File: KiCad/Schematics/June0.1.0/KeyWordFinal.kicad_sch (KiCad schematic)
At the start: 56 parts, among them J1 USB4105-GF-A, J2 Conn_01x02_Pin, J3 Conn_01x05_Pin, J4 MSD-10-C, U1 NRF52805-CAAA-R, U2 NPM1100-CAAA-R7, U3 TXB0104RUTR, U4 TPS62743YFPR, U5 MCP6142T-E/MS, Y1 32.868k, Y3 32M

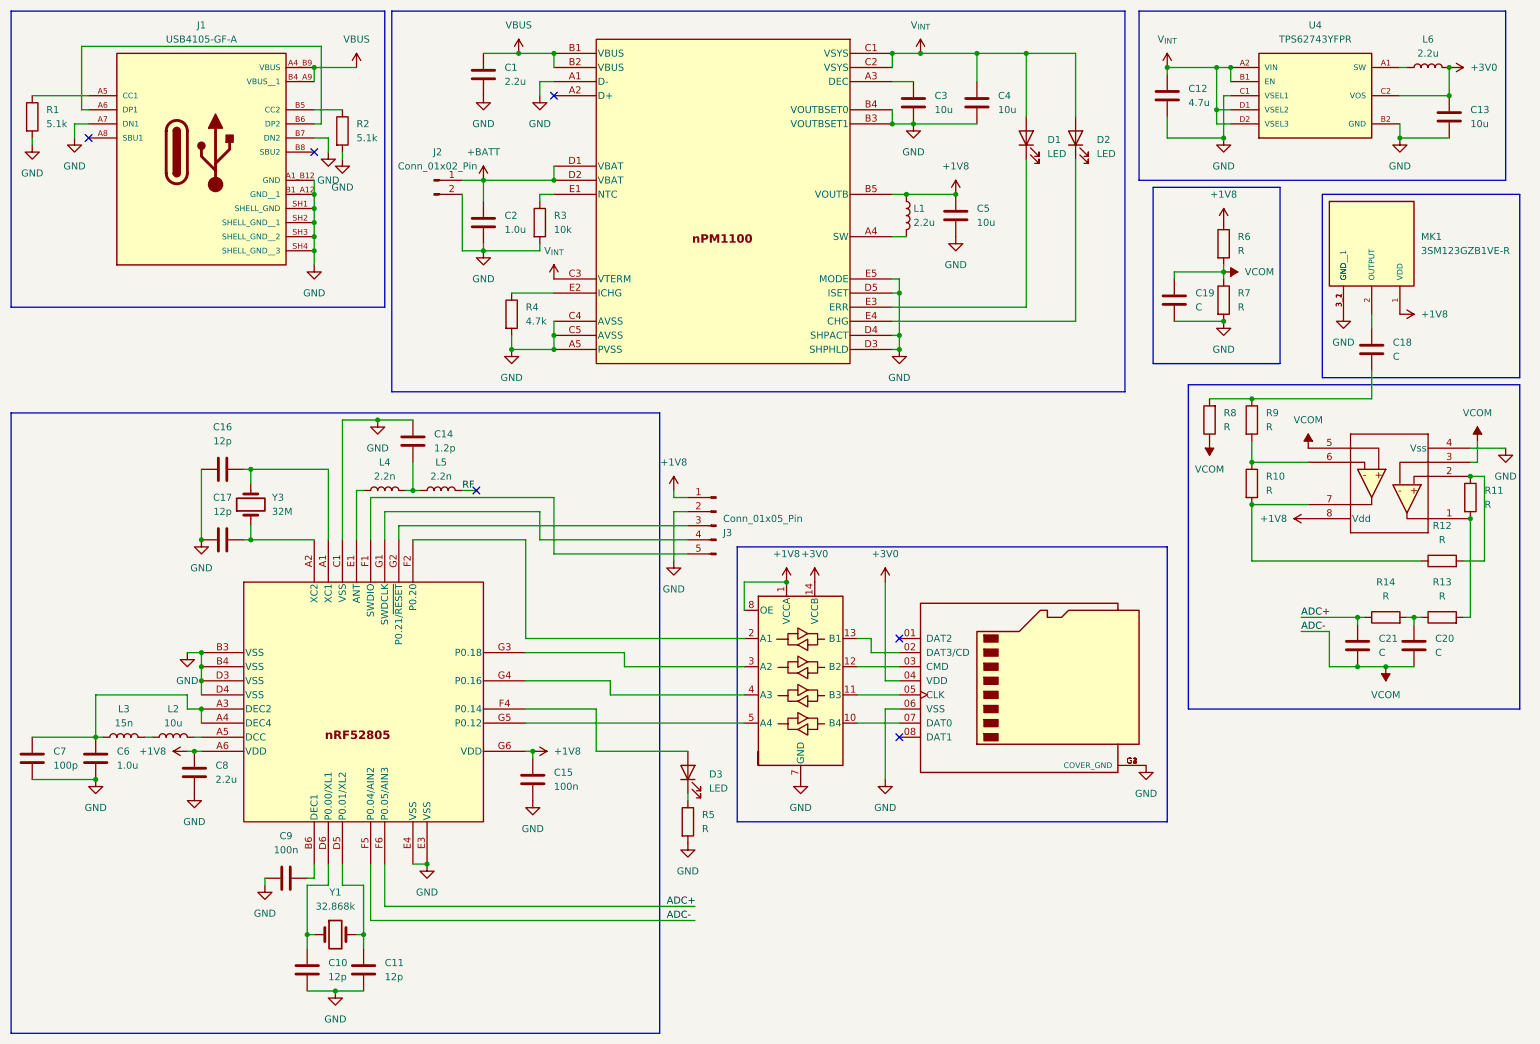
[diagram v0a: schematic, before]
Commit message: Added more 3d models, assigned footprints to components
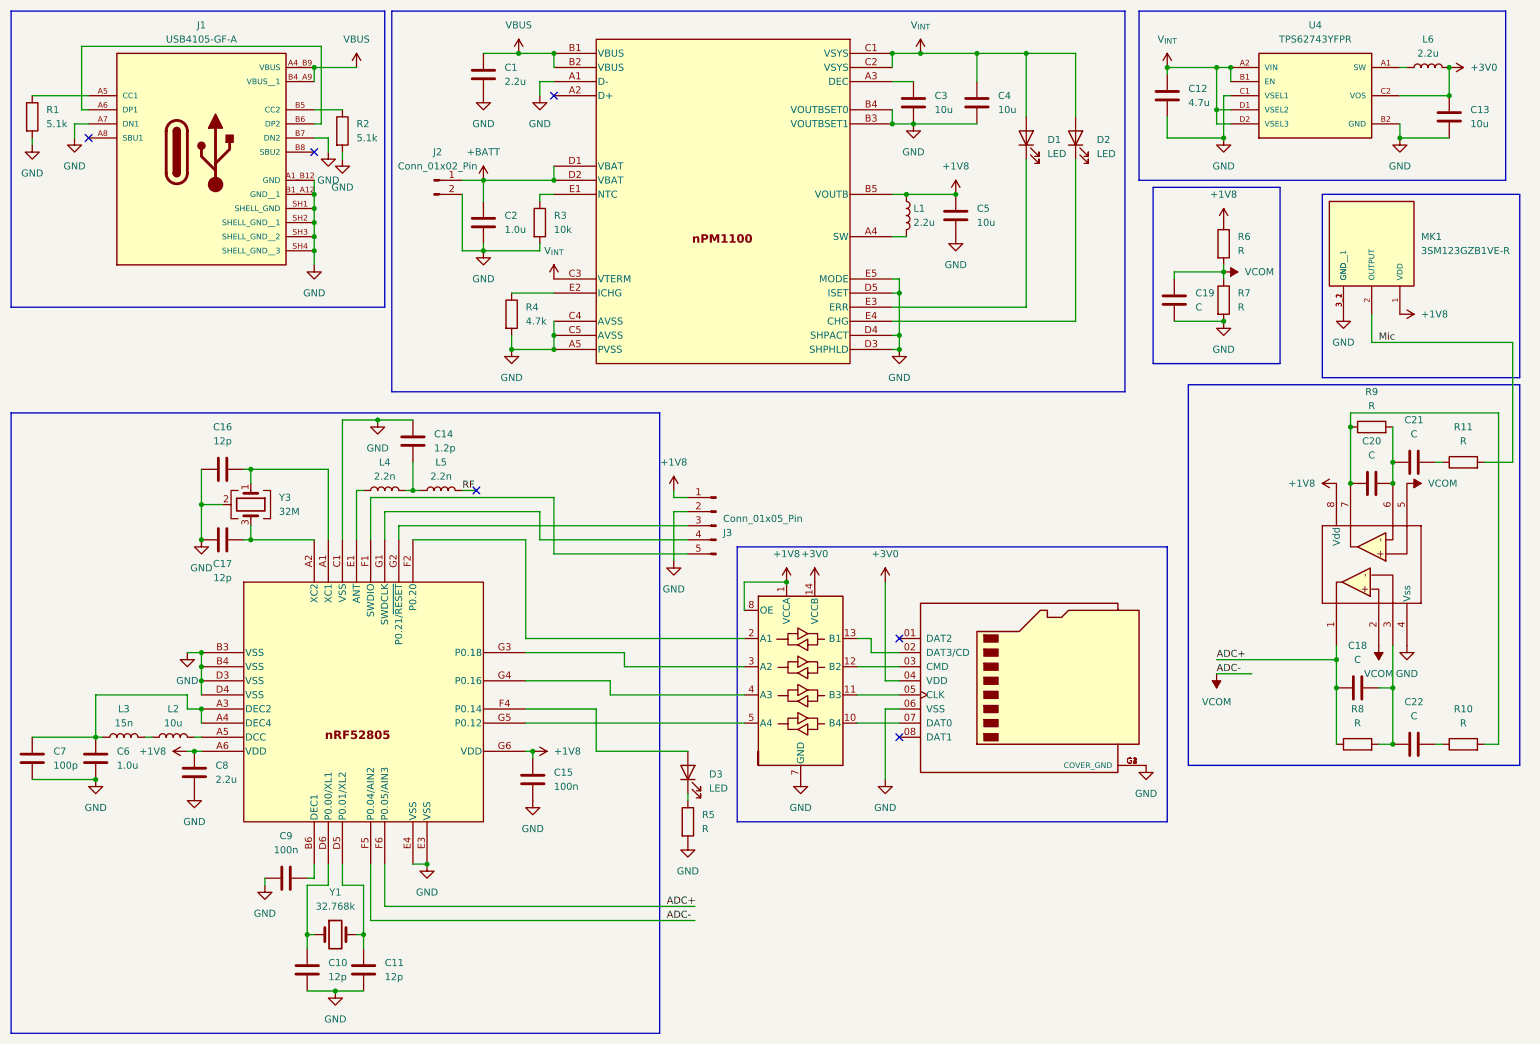
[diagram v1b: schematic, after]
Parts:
- removed R12, R13, R14: R, symbol Device:R
- removed Y3: 32M, symbol Device:Crystal
- added C22: C, Capacitor_SMD:C_0603_1608Metric, symbol Device:C
- added Y3: 32M, Crystal:Crystal_SMD_2016-4Pin_2.0x1.6mm, symbol Device:Crystal_GND24
- C1, C12, C13, C18, C19, C20, C21, C3, C4, C5: footprint (none) -> Capacitor_SMD:C_0603_1608Metric
- C10, C11, C14, C15, C16, C17, C2, C7, C9: footprint (none) -> Capacitor_SMD:C_0201_0603Metric
- C6, C8: footprint (none) -> Capacitor_SMD:C_0402_1005Metric
- D1, D2, D3: footprint (none) -> LED_SMD:LED_0603_1608Metric
- J1: footprint USB4105-GF-A:GCT_USB4105-GF-A -> projFootprints:USB4105
- J2: footprint (none) -> Connector_PinSocket_2.54mm:PinSocket_1x02_P2.54mm_Vertical
- J3: footprint (none) -> Connector_PinSocket_2.54mm:PinSocket_1x05_P2.54mm_Vertical
- J4: footprint MSD-10-C:CUI_MSD-10-C -> projFootprints:MSD-10-C
- L1, L6: footprint (none) -> Inductor_SMD:L_0805_2012Metric
- L2: footprint (none) -> Inductor_SMD:L_0603_1608Metric
- L3: footprint (none) -> Inductor_SMD:L_0402_1005Metric
- L4, L5: footprint (none) -> Inductor_SMD:L_0201_0603Metric
- MK1: footprint 3SM123GZB1VE-R:MIC_3SM123GZB1VE-R -> projFootprints:3SM123GZB1VE-R
- R1, R2, R3, R4: footprint (none) -> Resistor_SMD:R_0201_0603Metric
- R10, R11, R5, R6, R7, R8, R9: footprint (none) -> Resistor_SMD:R_0402_1005Metric
- U1: footprint WLCSP28_2p482x2p464_nRF52805_NOR -> projFootprints:NRF52805
- U2: footprint WLCSP_2p075X2p075_NOR -> projFootprints:NPM1100
- U3: footprint RUT12_TEX -> projFootprints:TXB0104
- U4: footprint TPS62743YFPR:BGA8N40P2X4_87X156X50 -> projFootprints:TPS62743
- U5: footprint MSOP8_MC_MCH -> Package_SO:MSOP-8_3x3mm_P0.65mm
- Y1: value 32.868k -> 32.768k; footprint (none) -> Crystal:Crystal_SMD_2012-2Pin_2.0x1.2mm
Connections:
- net ADC+: now also C18.1, R8.1, U5.1; no longer C21.1
- net GND: now also Y3.2 (G), Y3.4 (G)
- net VCOM: now also U5.2; no longer C20.2, C21.2, R8.1, U5.3
- net at C17.2, U1.A2 (XC2): now also Y3.3
- net at C16.2, U1.A1 (XC1): now also Y3.1
- net Mic: now reaches MK1.2 (OUTPUT)
- net Mic: now also R11.2; no longer C18.1
- net at C20.1: now also R10.2, R9.1, U5.7
- net at C18.2, R8.2: now also U5.3, C22.1; no longer R9.1
- net at R11.1: now also C21.2; no longer U5.2
- net at R9.2, U5.6: now also C20.2, C21.1; no longer R10.1
- new net: C22.2, R10.1
